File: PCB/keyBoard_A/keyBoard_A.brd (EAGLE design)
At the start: 184.3 x 152.4 mm, 314 parts, among them J1 J, J10 J, J11 J, J12 J, J13 J, J14 J, J15 J, J16 J, J17 J, J18 J, J19 J, J2 J, J20 J, J21 J, J22 J, J23 J, J24 J, J25 J, J26 J, J27 J, J28 J, J29 J, J3 J, J30 J, J31 J, J32 J, J33 J, J34 J, J35 J, J36 J, J37 J, J38 J, J39 J, J4 J, J40 J, J41 J, J42 J, J43 J, J44 J, J45 J, J46 J, J47 J, J48 J, J49 J, J5 J, J50 J, J51 J, J52 J, J53 J, J54 J, J55 J, J56 J, J57 J, J6 J, J7 J, J8 J, J9 J

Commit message: .
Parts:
- moved C17 23.7 mm to (149.2, 115.9)
- moved D15 23.7 mm to (117.2, 122.6)
- moved D19 23.7 mm to (91.8, 108.0)
- moved D21 23.7 mm to (131.4, 106.7)
- moved D22 23.7 mm to (151.1, 107.0)
- moved D30 23.7 mm to (181.3, 74.9)
- moved D33 23.7 mm to (129.5, 68.6)
- moved D35 23.7 mm to (167.6, 69.2)
- moved D36 23.7 mm to (181.3, 55.9)
- moved D39 23.7 mm to (111.1, 49.5)
- moved D40 23.7 mm to (131.8, 49.5)
- moved D41 23.7 mm to (151.1, 49.5)
- moved D43 23.7 mm to (111.1, 43.5)
- moved D44 23.7 mm to (139.1, 35.7)
- moved D45 23.7 mm to (163.2, 38.1)
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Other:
- board size 184.3 x 152.4 mm -> 184.3 x 134.6 mm

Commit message: add1
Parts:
- moved R8 1.27 mm to (61.8, 63.2)
- moved D44 0.63 mm to (138.4, 35.7)
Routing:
- net 3J3: track 59.3 -> 56.3 mm
- net L4: track 216.6 -> 214.8 mm
- net +5V: track 307.2 -> 308.5 mm
- net L5: track 233.5 -> 232.5 mm
- net N$147: track 41.3 -> 40.4 mm

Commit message: .
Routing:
- net N$148: track 43.2 -> 42.4 mm
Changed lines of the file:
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@@
 </element>
 <element name="JB44" library="detali" package="SJ" value="" x="104.14" y="24.765"/>
-<element name="JB45" library="detali" package="SJ" value="" x="125.73" y="24.765"/>
+<element name="JB45" library="detali" package="SJ" value="" x="125.73" y="24.765" smashed="yes">
+<attribute name="NAME" x="128.651" y="25.908" size="1.27" layer="26" ratio="10" rot="MR0"/>
+<attribute name="VALUE" x="125.3299" y="24.765" size="0.02" layer="28" rot="MR0"/>
+</element>
 <element name="JB46" library="detali" package="SJ" value="" x="164.1475" y="25.0825" smashed="yes" rot="R90">
 <attribute name="NAME" x="162.814" y="22.987" size="1.27" layer="26" ratio="10" rot="MR180"/>
@@
 <attribute name="VALUE" x="70.1675" y="19.6024" size="0.02" layer="28" rot="MR270"/>
 </element>
-<element name="JA44" library="detali" package="SJ" value="" x="97.4725" y="20.16125" rot="R90"/>
-<element name="JA45" library="detali" package="SJ" value="" x="118.745" y="20.16125" rot="R90"/>
+<element name="JA44" library="detali" package="SJ" value="" x="97.4725" y="20.16125" smashed="yes" rot="R90">
+<attribute name="NAME" x="100.1395" y="21.81225" size="1.27" layer="26" ratio="10" rot="MR270"/>
+<attribute name="VALUE" x="97.4725" y="19.76115" size="0.02" layer="28" rot="MR270"/>
+</element>
+<element name="JA45" library="detali" package="SJ" value="" x="118.745" y="20.16125" smashed="yes" rot="R90">
+<attribute name="NAME" x="121.412" y="21.81225" size="1.27" layer="26" ratio="10" rot="MR270"/>
+<attribute name="VALUE" x="118.745" y="19.76115" size="0.02" layer="28" rot="MR270"/>
+</element>
 <element name="JA46" library="detali" package="SJ" value="" x="150.1775" y="20.6375" smashed="yes" rot="R90">
 <attribute name="NAME" x="152.3365" y="19.4945" size="1.27" layer="26" ratio="10" rot="MR180"/>
@@
 <wire x1="152.9225" y1="36.0825" x2="163.195" y2="36.4" width="1.016" layer="16"/>
 <wire x1="149.86" y1="33.655" x2="152.9225" y2="36.0825" width="0.6096" layer="16"/>
-<wire x1="129.8575" y1="29.845" x2="126.8095" y2="28.702" width="0.6096" layer="16"/>
-<wire x1="126.8095" y1="28.702" x2="126.492" y2="24.765" width="0.6096" layer="16"/>
 <wire x1="129.8575" y1="29.845" x2="146.685" y2="29.845" width="0.6096" layer="16"/>
 <wire x1="146.685" y1="29.845" x2="149.86" y2="33.655" width="0.6096" layer="16"/>
+<wire x1="126.492" y1="24.765" x2="126.492" y2="26.4795" width="0.6096" layer="16"/>
+<wire x1="126.492" y1="26.4795" x2="129.8575" y2="29.845" width="0.6096" layer="16"/>
 </signal>
 <signal name="N$149">

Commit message: .
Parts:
- moved D46 4.36 mm to (168.4, 30.2), turned to 0 degrees
- moved JA46 3.42 mm to (148.9, 23.8), turned to 0 degrees
- moved D12 1.80 mm to (90.5, 43.2)
- moved JB46 1.27 mm to (165.4, 25.1), turned to 0 degrees
- moved JB37 0.63 mm to (67.0, 42.2)
- moved D10 0.32 mm to (13.7, 43.2)
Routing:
- net 8: track 149.6 -> 144.7 mm
- net N$149: track 1.82 -> 5.31 mm
- net GND: track 246.0 -> 242.8 mm
- net N$56: track 34.9 -> 32.1 mm
- net 3J3: track 56.3 -> 53.9 mm
- net L6: track 166.3 -> 164.3 mm
- net N$140: track 20.0 -> 18.0 mm
- net L5: track 232.5 -> 234.5 mm
- net 4J3: track 32.1 -> 30.7 mm
- net N$148: track 42.4 -> 41.4 mm
- net L1: track 321.5 -> 320.8 mm
- net N$115: track 3.59 -> 4.30 mm
- net L4: track 214.8 -> 214.2 mm
- net 1J3: track 38.6 -> 39.1 mm
- removed copper zone on layer 16, net N$181
- removed copper zone on layer 16, net N$239
- removed copper zone on layer 16, net N$240
- removed copper zone on layer 16, net N$241

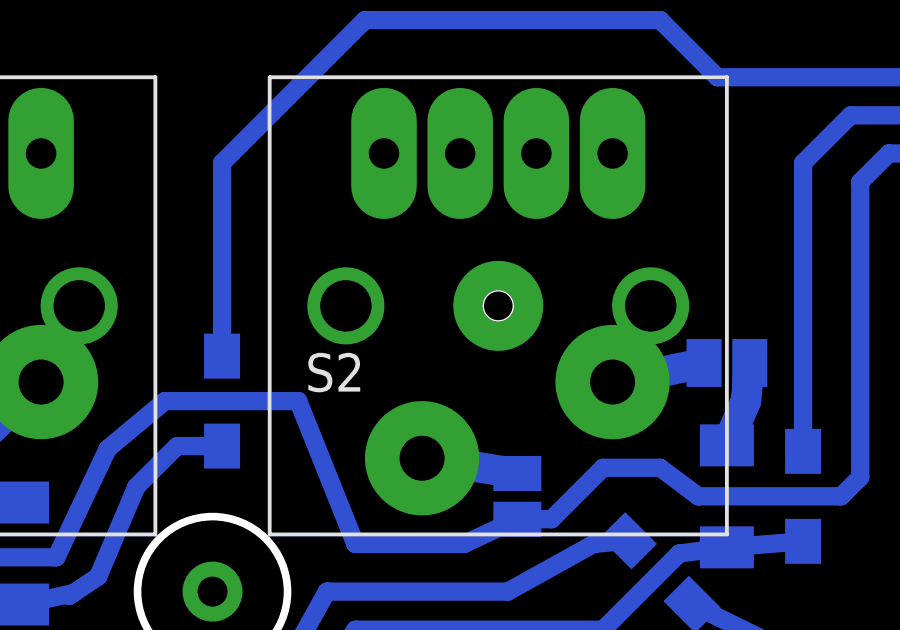
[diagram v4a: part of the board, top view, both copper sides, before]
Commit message: kb swap
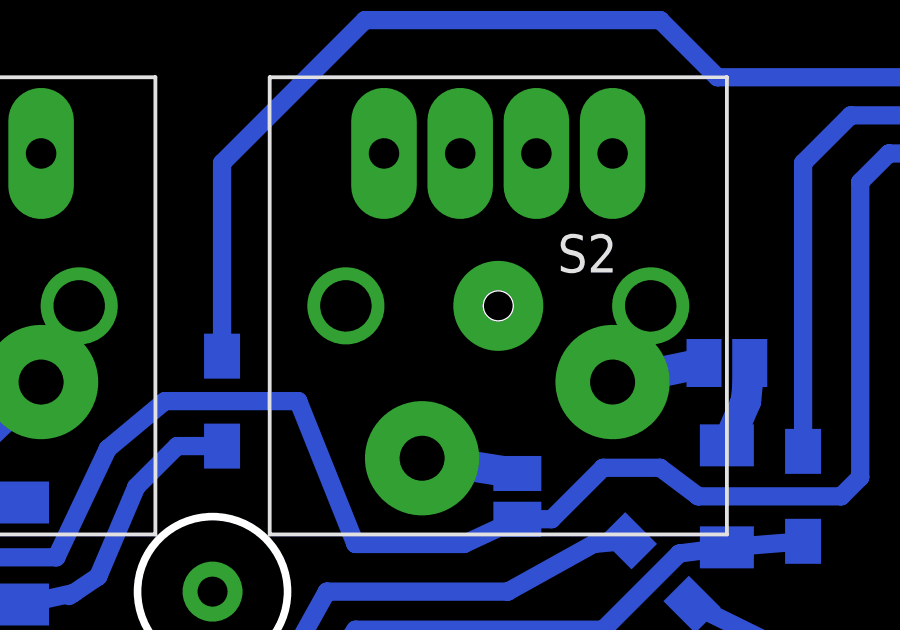
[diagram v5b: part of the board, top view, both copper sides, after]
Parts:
- S1: value Scroll Lock -> ESC
- S2: value ESC -> Scroll Lock
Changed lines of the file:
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@@
 <?xml version="1.0" encoding="utf-8"?>
 <!DOCTYPE eagle SYSTEM "eagle.dtd">
-<eagle version="6.4">
+<eagle version="6.3">
 <drawing>
 <settings>
@@
 <circle x="168.91" y="55.88" radius="2.5" width="0.254" layer="21"/>
 <circle x="168.91" y="120.65" radius="2.5" width="0.254" layer="20"/>
-<dimension x1="3.65125" y1="147.0025" x2="187.96" y2="146.20875" x3="95.805625" y3="152.7175" textsize="3.5" layer="21" dtype="horizontal"/>
+<dimension x1="3.65125" y1="147.0025" x2="187.96" y2="146.20875" x3="95.805625" y3="152.7175" layer="21" dtype="horizontal"/>
 <wire x1="182.40375" y1="14.605" x2="182.40375" y2="33.9725" width="0.2" layer="20"/>
 <wire x1="182.40375" y1="33.9725" x2="182.40375" y2="37.1475" width="0.2" layer="20"/>
@@
 <wire x1="64.77" y1="118.58625" x2="52.705" y2="118.58625" width="0.2" layer="20"/>
 <wire x1="52.705" y1="118.58625" x2="52.705" y2="133.82625" width="0.2" layer="20"/>
-<dimension x1="182.72125" y1="11.43" x2="188.595" y2="146.05" x3="195.58" y3="78.74" textsize="3.5" layer="21" dtype="vertical"/>
+<dimension x1="182.72125" y1="11.43" x2="188.595" y2="146.05" x3="195.58" y3="78.74" layer="21" dtype="vertical"/>
 <circle x="63.8175" y="74.93" radius="2.5" width="0.254" layer="20"/>
 <circle x="68.8975" y="93.98" radius="2.5" width="0.254" layer="20"/>
@@
 <wire x1="185.57875" y1="37.1475" x2="182.40375" y2="33.9725" width="0.2" layer="20" curve="90"/>
 <wire x1="184.785" y1="37.1475" x2="187.96" y2="40.3225" width="0.2" layer="20" curve="90"/>
-<dimension x1="3.65125" y1="12.54125" x2="182.40375" y2="11.1125" x3="93.0275" y3="3.81" textsize="3.5" layer="21" dtype="horizontal"/>
+<dimension x1="3.65125" y1="12.54125" x2="182.40375" y2="11.1125" x3="93.0275" y3="3.81" layer="21" dtype="horizontal"/>
 </plain>
 <attributes>
@@
 </autorouter>
 <elements>
-<element name="S1" library="cherrymx" package="CHERRY-MX-4P" value="Scroll Lock" x="19.685" y="130.175" smashed="yes" rot="R180">
+<element name="S1" library="cherrymx" package="CHERRY-MX-4P" value="ESC" x="19.685" y="130.175" smashed="yes" rot="R180">
 <attribute name="NAME" x="14.605" y="133.0325" size="1.27" layer="25" rot="R180"/>
 <attribute name="VALUE" x="20.955" y="128.27" size="1.27" layer="27" rot="R180"/>
 </element>
-<element name="S2" library="cherrymx" package="CHERRY-MX-4P" value="ESC" x="38.735" y="130.175" smashed="yes" rot="R180">
-<attribute name="NAME" x="34.29" y="128.5875" size="1.27" layer="25" rot="R180"/>
-<attribute name="VALUE" x="40.005" y="128.27" size="1.27" layer="27" rot="R180"/>
+<element name="S2" library="cherrymx" package="CHERRY-MX-4P" value="Scroll Lock" x="38.735" y="130.175" smashed="yes" rot="R180">
+<attribute name="NAME" x="42.70375" y="132.55625" size="1.27" layer="25" rot="R180"/>
+<attribute name="VALUE" x="40.48125" y="128.27" size="1.27" layer="27" rot="R180"/>
 </element>
 <element name="S3" library="cherrymx" package="CHERRY-MX-4P" value="Ins" x="19.685" y="111.125" smashed="yes" rot="R180">

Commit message: .
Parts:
- R3: value 10k -> 0
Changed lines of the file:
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@@
 <element name="S1" library="cherrymx" package="CHERRY-MX-4P" value="ESC" x="19.685" y="130.175" smashed="yes" rot="R180">
 <attribute name="NAME" x="14.605" y="133.0325" size="1.27" layer="25" rot="R180"/>
-<attribute name="VALUE" x="20.955" y="128.27" size="1.27" layer="27" rot="R180"/>
+<attribute name="VALUE" x="17.30375" y="128.5875" size="1.27" layer="27" rot="R180"/>
 </element>
 <element name="S2" library="cherrymx" package="CHERRY-MX-4P" value="Scroll Lock" x="38.735" y="130.175" smashed="yes" rot="R180">
 <attribute name="NAME" x="42.70375" y="132.55625" size="1.27" layer="25" rot="R180"/>
-<attribute name="VALUE" x="40.48125" y="128.27" size="1.27" layer="27" rot="R180"/>
+<attribute name="VALUE" x="39.52875" y="133.0325" size="1.27" layer="27" rot="R180"/>
 </element>
 <element name="S3" library="cherrymx" package="CHERRY-MX-4P" value="Ins" x="19.685" y="111.125" smashed="yes" rot="R180">
@@
 <attribute name="VALUE" x="29.341515625" y="37.750590625" size="1.27" layer="28" rot="MR225"/>
 </element>
-<element name="R3" library="rcl" package="R1206W" value="10k" x="29.21" y="40.64" smashed="yes" rot="MR90">
+<element name="R3" library="rcl" package="R1206W" value="0" x="29.21" y="40.64" smashed="yes" rot="MR90">
 <attribute name="NAME" x="33.02" y="39.37" size="1.27" layer="26" rot="MR0"/>
 <attribute name="VALUE" x="26.67" y="38.735" size="1.27" layer="28" rot="MR90"/>

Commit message: .
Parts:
- added U$47, U$53: (no value), kbmx:18X52
- added U$48, U$50, U$51: (no value), kbmx:18X23
- added U$49, U$52: (no value), kbmx:18X18
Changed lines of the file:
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@@
 <setting verticaltext="up"/>
 </settings>
-<grid distance="6.25" unitdist="mil" unit="mil" style="lines" multiple="1" display="yes" altdistance="0.025" altunitdist="inch" altunit="inch"/>
+<grid distance="25" unitdist="mil" unit="mil" style="lines" multiple="1" display="yes" altdistance="0.025" altunitdist="inch" altunit="inch"/>
 <layers>
 <layer number="1" name="Top" color="4" fill="1" visible="yes" active="yes"/>
@@
 <layer number="26" name="bNames" color="7" fill="1" visible="yes" active="yes"/>
 <layer number="27" name="tValues" color="7" fill="1" visible="yes" active="yes"/>
-<layer number="28" name="bValues" color="7" fill="1" visible="no" active="yes"/>
+<layer number="28" name="bValues" color="7" fill="1" visible="yes" active="yes"/>
 <layer number="29" name="tStop" color="7" fill="3" visible="no" active="yes"/>
 <layer number="30" name="bStop" color="7" fill="6" visible="no" active="yes"/>
@@
 <wire x1="185.57875" y1="37.1475" x2="182.40375" y2="33.9725" width="0.2" layer="20" curve="90"/>
 <wire x1="184.785" y1="37.1475" x2="187.96" y2="40.3225" width="0.2" layer="20" curve="90"/>
-<dimension x1="3.65125" y1="12.54125" x2="182.40375" y2="11.1125" x3="93.0275" y3="3.81" textsize="3.5" layer="21" dtype="horizontal"/>
+<dimension x1="3.65125" y1="12.54125" x2="182.40375" y2="11.1125" x3="93.0275" y3="-34.44875" textsize="3.5" layer="21" dtype="horizontal"/>
+<dimension x1="140.335" y1="-20.47875" x2="106.9975" y2="-24.60625" x3="123.66625" y3="162.08375" textsize="1.778" layer="21" dtype="horizontal"/>
+<dimension x1="140.335" y1="-22.225" x2="142.875" y2="5.08" x3="141.605" y3="-26.67" textsize="1.778" layer="1" dtype="horizontal"/>
 </plain>
 <attributes>
@@
 <element name="STAB_LSP" library="kbmxco" package="ZEALIOS-PCB_2U" value="STAB" x="156.21" y="27.305" rot="R180"/>
 <element name="STAB_LSH" library="kbmxco" package="ZEALIOS-PCB_2U" value="STAB" x="73.66" y="46.355" rot="R180"/>
+<element name="U$47" library="kbmx" package="18X52" value="" x="142.875" y="-0.635"/>
+<element name="U$48" library="kbmx" package="18X23" value="" x="103.8225" y="-0.635"/>
+<element name="U$49" library="kbmx" package="18X18" value="" x="56.515" y="0.635"/>
+<element name="U$50" library="kbmx" package="18X23" value="" x="79.6925" y="-0.635"/>
+<element name="U$51" library="kbmx" package="18X23" value="" x="80.9625" y="-19.685"/>
+<element name="U$52" library="kbmx" package="18X18" value="" x="102.235" y="-18.415"/>
+<element name="U$53" library="kbmx" package="18X52" value="" x="140.335" y="-19.685"/>
 </elements>
 <signals>
